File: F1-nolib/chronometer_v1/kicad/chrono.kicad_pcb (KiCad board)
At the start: 2 copper layers, 97.5 x 59.5 mm, 90 parts, among them J1 Power 12V, J10 LIDAR, J11 Bluetooth, J12 SWD, J2 GPS_ext, J3 PPS, J4 Ext_trig1, J5 Ext_trig0, J6 USB_B_Mini, J7 Ext_trig2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

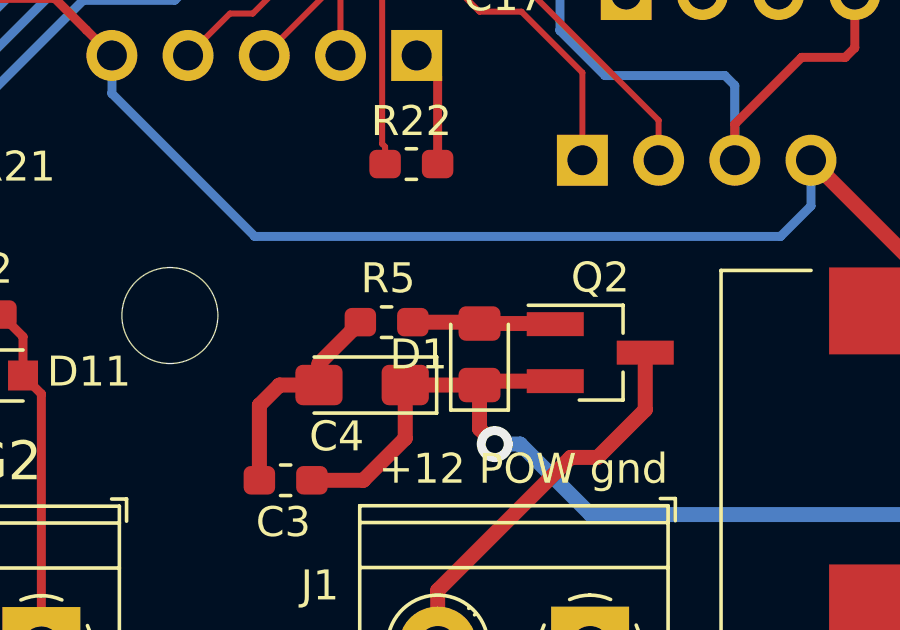
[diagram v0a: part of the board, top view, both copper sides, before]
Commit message: Add SPI DMA Tx example
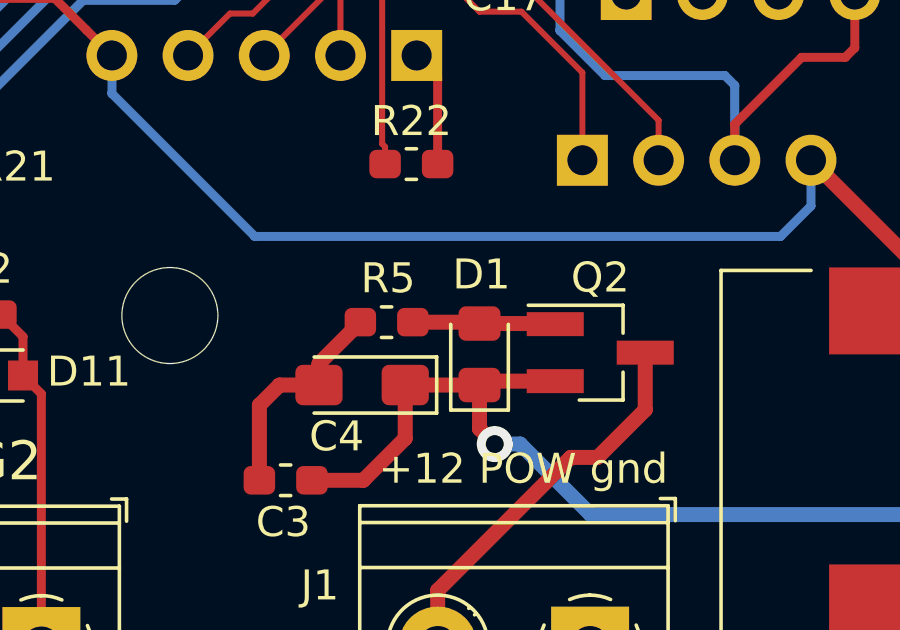
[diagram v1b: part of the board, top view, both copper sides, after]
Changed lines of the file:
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@@
-(kicad_pcb (version 20171130) (host pcbnew 5.1.0)
+(kicad_pcb (version 20171130) (host pcbnew "(6.0.0-rc1-dev-1613-ga55d9819b)")
   (general
     (thickness 1.6)
@@
   )
   (setup
-    (last_trace_width 0.5)
+    (last_trace_width 0.2)
     (user_trace_width 0.2)
     (user_trace_width 0.3)
@@
     (visible_elements FFFFFF7F)
     (pcbplotparams
-      (layerselection 0x010f0_ffffffff)
+      (layerselection 0x01010_7ffffffe)
       (usegerberextensions false)
       (usegerberattributes false)
@@
       (padsonsilk false)
       (subtractmaskfromsilk false)
-      (outputformat 1)
-      (mirror false)
+      (outputformat 5)
+      (mirror true)
       (drillshape 0)
       (scaleselection 1)
@@
     (tags "diode handsolder")
     (attr smd)
-    (fp_text reference D1 (at -0.009 -2.032 -180) (layer F.SilkS)
-      (effects (font (size 1 1) (thickness 0.15)))
-    )
+    (fp_text reference D1 (at 2.658 0.0635 -180) (layer F.SilkS)
+      (effects (font (size 1 1) (thickness 0.15)))
+    )
